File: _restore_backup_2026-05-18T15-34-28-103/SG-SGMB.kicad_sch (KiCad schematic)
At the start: 0 parts

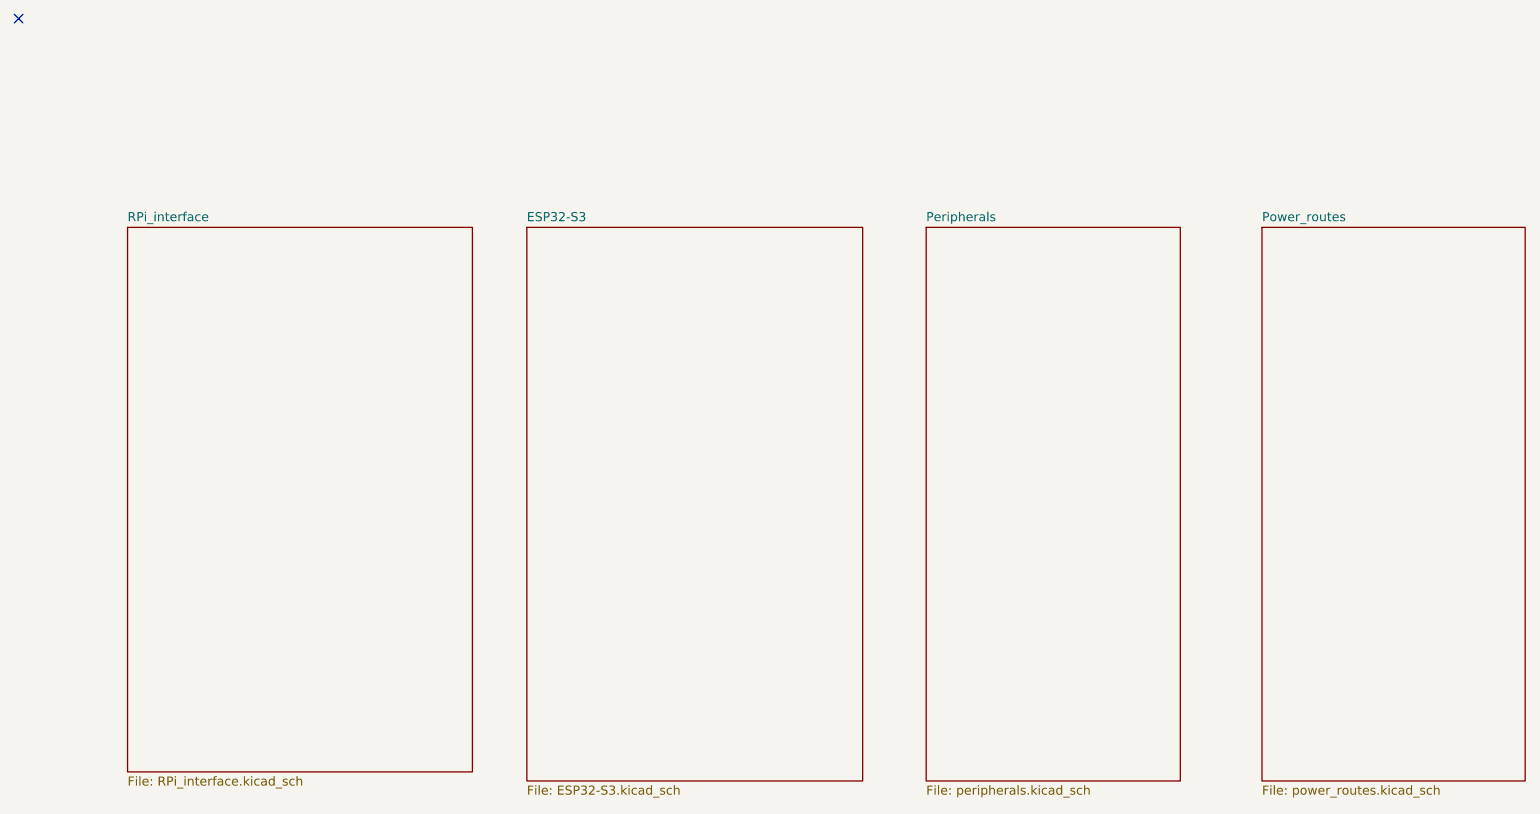
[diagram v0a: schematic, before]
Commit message: feat: added hierarchical folder system for better readability. Halfway finishing the motherboard. Power Routes will be next.
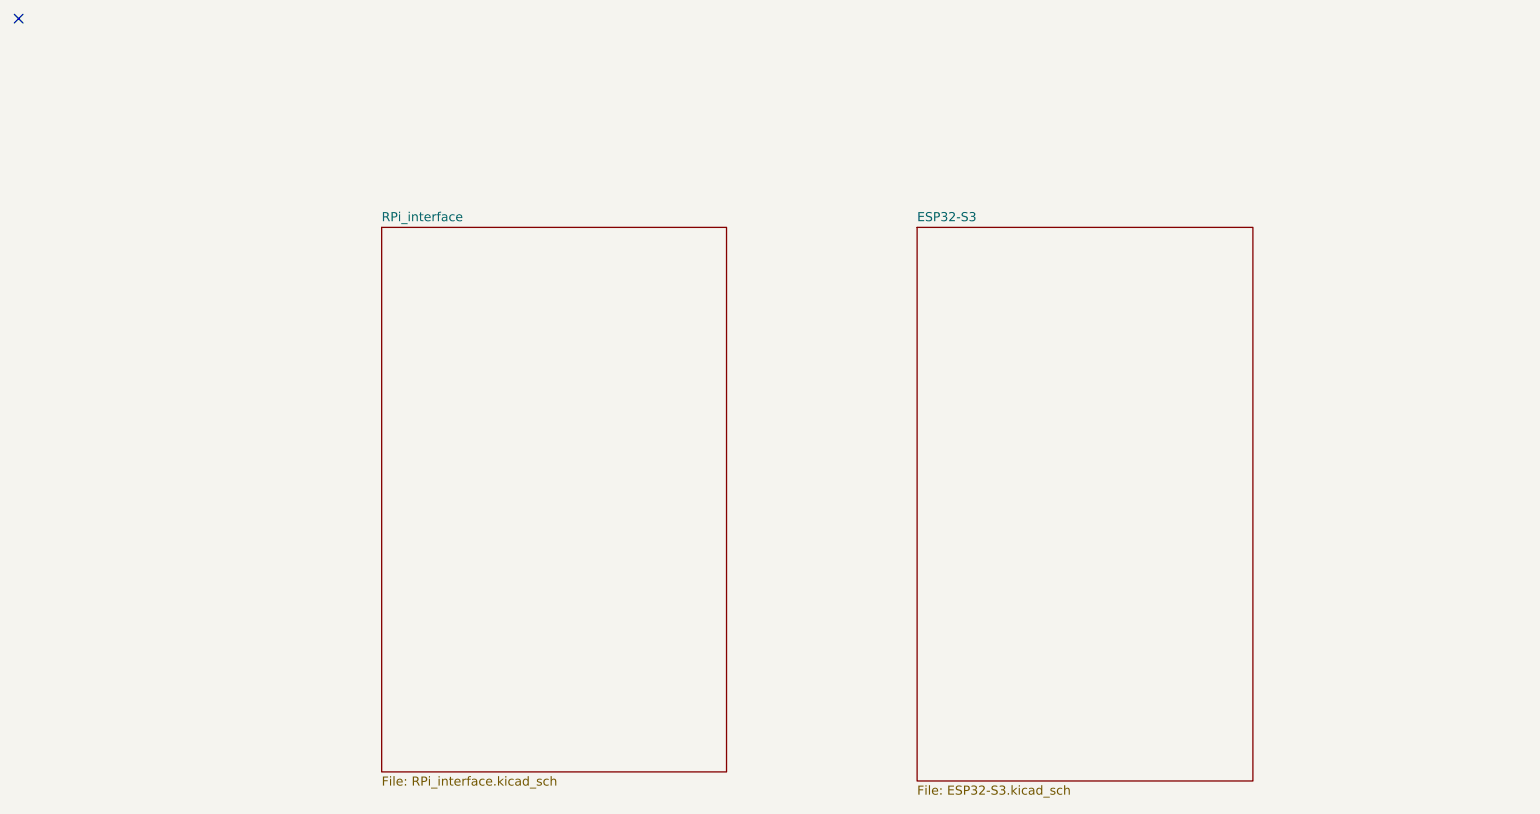
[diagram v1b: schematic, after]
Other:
- removed sheet Peripherals
- removed sheet Power_routes
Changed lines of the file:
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@@
 	)
 	(sheet
-		(at 77.47 40.64)
+		(at 132.08 40.64)
 		(size 46.99 77.47)
 		(exclude_from_sim no)
@@
 		)
 		(property "Sheetname" "ESP32-S3"
-			(at 77.47 39.9284 0)
+			(at 132.08 39.9284 0)
 			(show_name no)
 			(do_not_autoplace no)
@@
 		)
 		(property "Sheetfile" "ESP32-S3.kicad_sch"
-			(at 77.47 118.6946 0)
+			(at 132.08 118.6946 0)
 			(show_name no)
 			(do_not_autoplace no)
@@
 	)
 	(sheet
-		(at 133.35 40.64)
-		(size 35.56 77.47)
-		(exclude_from_sim no)
-		(in_bom yes)
-		(on_board yes)
-		(dnp no)
-		(fields_autoplaced yes)
-		(stroke
-			(width 0.1524)
-			(type solid)
-		)
-		(fill
-			(color 0 0 0 0)
-		)
-		(property "Sheetname" "Peripherals"
-			(at 133.35 39.9284 0)
-			(show_name no)
-			(do_not_autoplace no)
-			(effects
-				(font
-					(size 1.27 1.27)
-				)
-				(justify left bottom)
-			)
-		)
-		(property "Sheetfile" "peripherals.kicad_sch"
-			(at 133.35 118.6946 0)
-			(show_name no)
-			(do_not_autoplace no)
-			(effects
-				(font
-					(size 1.27 1.27)
-				)
-				(justify left top)
-			)
-		)
-		(instances
-			(project "SG-SGMB"
-				(path "/b172e4a5-d9fb-488b-8521-d5778a7acb4c"
-					(page "4")
-				)
-			)
-		)
-	)
-	(sheet
-		(at 21.59 40.64)
+		(at 57.15 40.64)
 		(size 48.26 76.2)
 		(exclude_from_sim no)
@@
 		)
 		(property "Sheetname" "RPi_interface"
-			(at 21.59 39.9284 0)
+			(at 57.15 39.9284 0)
 			(show_name no)
 			(do_not_autoplace no)
@@
 		)
 		(property "Sheetfile" "RPi_interface.kicad_sch"
-			(at 21.59 117.4246 0)
+			(at 57.15 117.4246 0)
 			(show_name no)
 			(do_not_autoplace no)
@@
 				)
 			)
-		)
-	)
-	(sheet
-		(at 180.34 40.64)
-		(size 36.83 77.47)
-		(exclude_from_sim no)
-		(in_bom yes)
-		(on_board yes)
-		(dnp no)
-		(fields_autoplaced yes)
-		(stroke
-			(width 0.1524)
-			(type solid)
-		)
-		(fill
-			(color 0 0 0 0)
-		)
-		(property "Sheetname" "Power_routes"
-			(at 180.34 39.9284 0)
-			(show_name no)
-			(do_not_autoplace no)
-			(effects
-				(font
-					(size 1.27 1.27)
-				)
-				(justify left bottom)
-			)
-		)
-		(property "Sheetfile" "power_routes.kicad_sch"
-			(at 180.34 118.6946 0)
-			(show_name no)
-			(do_not_autoplace no)
-			(effects
-				(font
-					(size 1.27 1.27)
-				)
-				(justify left top)
-			)
-		)
-		(instances
-			(project "SG-SGMB"
-				(path "/b172e4a5-d9fb-488b-8521-d5778a7acb4c"
-					(page "5")
-				)
-			)
